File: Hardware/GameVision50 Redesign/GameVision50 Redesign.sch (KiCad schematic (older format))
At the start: 26 parts

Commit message: annotated and assigned footprints
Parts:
- C1, C4: renamed from C?; footprint (none) -> Capacitor_SMD:C_0805_2012Metric
- C10, C2, C3, C7, C8, C9: renamed from C?; footprint (none) -> Capacitor_SMD:C_0402_1005Metric
- C5, C6: renamed from C?; footprint (none) -> Capacitor_SMD:C_0603_1608Metric
- J1, J6: renamed from J?; footprint (none) -> Connector_PinHeader_2.54mm:PinHeader_1x04_P2.54mm_Vertical
- J2: renamed from J?; footprint (none) -> Connector_PinHeader_2.54mm:PinHeader_1x03_P2.54mm_Vertical
- J3: renamed from J?; footprint (none) -> Connector_USB:USB_Mini-B_Lumberg_2486_01_Horizontal
- J4: renamed from J?; footprint (none) -> Connector_PinHeader_2.54mm:PinHeader_1x05_P2.54mm_Vertical
- J5: renamed from J?; footprint (none) -> Connector_JST:JST_XH_B7B-XH-A_1x07_P2.50mm_Vertical
- JP1: renamed from JP?; footprint (none) -> Jumper:SolderJumper-2_P1.3mm_Open_TrianglePad1.0x1.5mm
- R1, R2, R3, R4: renamed from R?; footprint (none) -> Resistor_SMD:R_0402_1005Metric
- R5, R6: renamed from R?; footprint (none) -> Resistor_SMD:R_0603_1608Metric
- Y1: renamed from Y?; footprint (none) -> Crystal:Crystal_SMD_5032-2Pin_5.0x3.2mm
- gave numbers to parts that had none: 2

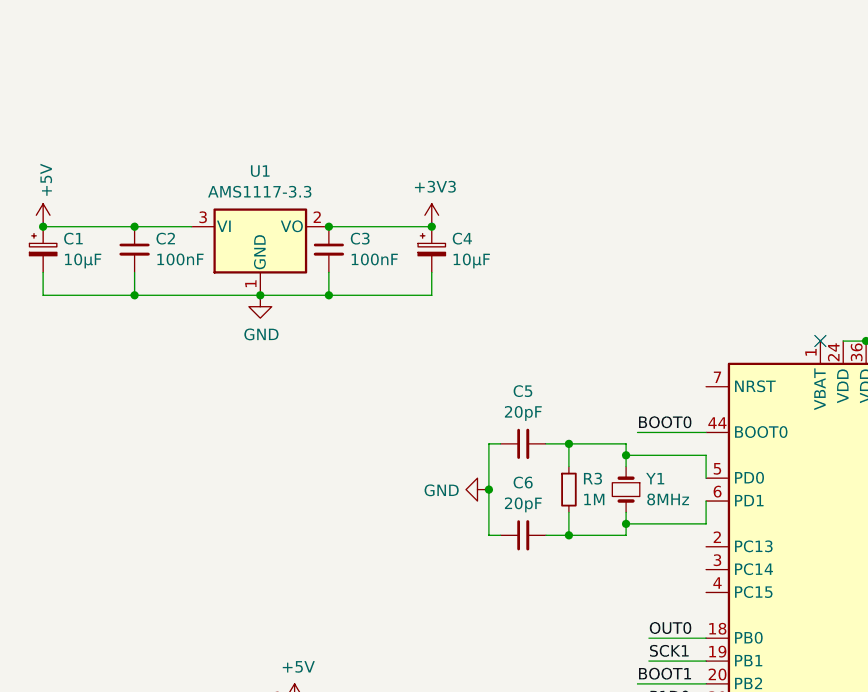
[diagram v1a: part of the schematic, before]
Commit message: added power-on reset IC with pull-up and bypass cap
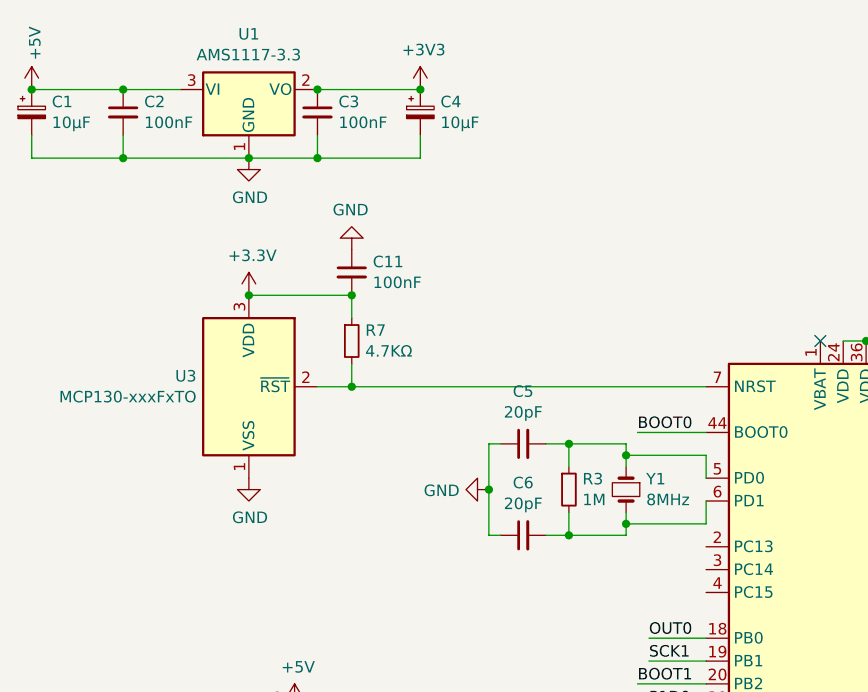
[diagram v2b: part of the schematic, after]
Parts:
- added C11: 100nF, Capacitor_SMD:C_0402_1005Metric, symbol Device:C_Small
- added R7: 4.7KΩ, Resistor_SMD:R_0402_1005Metric, symbol Device:R_Small
- added U3: MCP130-xxxFxTO, Package_TO_SOT_THT:TO-92_Inline, symbol Power_Supervisor:MCP130-xxxFxTO
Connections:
- net +3V3: now also C11.2, R7.1, U3.3 (VDD)
- net GND: now also C11.1, U3.1 (VSS)
- net at U2.7 (NRST): now also R7.2, U3.2 (~RST)
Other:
- moved on the sheet: C1, C2, C3, C4, U1
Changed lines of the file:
@@
 POWER
-$Comp
-L power:+5V #PWR0104
-U 1 1 5EDC21FE
-P 1950 1500
-F 0 "#PWR0104" H 1950 1350 50  0001 C CNN
-F 1 "+5V" V 1965 1628 50  0000 L CNN
-F 2 "" H 1950 1500 50  0001 C CNN
-F 3 "" H 1950 1500 50  0001 C CNN
-	1    1950 1500
-	1    0    0    -1
-$EndComp
-$Comp
-L power:+3V3 #PWR0105
-U 1 1 5EDC2D33
-P 3650 1500
-F 0 "#PWR0105" H 3650 1350 50  0001 C CNN
-F 1 "+3V3" H 3665 1673 50  0000 C CNN
-F 2 "" H 3650 1500 50  0001 C CNN
-F 3 "" H 3650 1500 50  0001 C CNN
-	1    3650 1500
-	1    0    0    -1
-$EndComp
-$Comp
-L Device:CP_Small C1
-U 1 1 5EDC44C0
-P 1950 1600
-F 0 "C1" H 2038 1646 50  0000 L CNN
-F 1 "10μF" H 2038 1555 50  0000 L CNN
-F 2 "Capacitor_SMD:C_0805_2012Metric" H 1950 1600 50  0001 C CNN
-F 3 "~" H 1950 1600 50  0001 C CNN
-F 4 "C15850" H 1950 1600 50  0001 C CNN "LCSC"
-	1    1950 1600
-	1    0    0    -1
-$EndComp
 $Comp
 L Connector_Generic:Conn_01x05 J4
@@
 Text Label 4550 3900 0    50   ~ 0
 RESET
-$Comp
-L Device:C_Small C2
-U 1 1 5EE03D1D
-P 2350 1600
-F 0 "C2" H 2442 1646 50  0000 L CNN
-F 1 "100nF" H 2442 1555 50  0000 L CNN
-F 2 "Capacitor_SMD:C_0402_1005Metric" H 2350 1600 50  0001 C CNN
-F 3 "~" H 2350 1600 50  0001 C CNN
-F 4 "C1525" H 2350 1600 50  0001 C CNN "LCSC"
-	1    2350 1600
-	1    0    0    -1
-$EndComp
-Wire Wire Line
-	3200 1800 3200 1700
-Wire Wire Line
-	3200 1800 3650 1800
-Wire Wire Line
-	3650 1800 3650 1700
-Connection ~ 3200 1800
-Connection ~ 2900 1800
-Wire Wire Line
-	2900 1800 3200 1800
-$Comp
-L power:GND #PWR0114
-U 1 1 5EDC383E
-P 2900 1800
-F 0 "#PWR0114" H 2900 1550 50  0001 C CNN
-F 1 "GND" H 2905 1627 50  0000 C CNN
-F 2 "" H 2900 1800 50  0001 C CNN
-F 3 "" H 2900 1800 50  0001 C CNN
-	1    2900 1800
-	1    0    0    -1
-$EndComp
-$Comp
-L Regulator_Linear:AMS1117-3.3 U1
-U 1 1 5EDBF4D0
-P 2900 1500
-F 0 "U1" H 2900 1742 50  0000 C CNN
-F 1 "AMS1117-3.3" H 2900 1651 50  0000 C CNN
-F 2 "Package_TO_SOT_SMD:SOT-223-3_TabPin2" H 2900 1700 50  0001 C CNN
-F 3 "http://www.advanced-monolithic.com/pdf/ds1117.pdf" H 3000 1250 50  0001 C CNN
-	1    2900 1500
-	1    0    0    -1
-$EndComp
-Wire Wire Line
-	2350 1700 2350 1800
-Wire Wire Line
-	2350 1800 2900 1800
-Wire Wire Line
-	1950 1700 1950 1800
-Wire Wire Line
-	1950 1800 2350 1800
-Connection ~ 2350 1800
-Wire Wire Line
-	1950 1500 2350 1500
-Connection ~ 1950 1500
-Connection ~ 2350 1500
-Wire Wire Line
-	2350 1500 2600 1500
-Wire Wire Line
-	3200 1500 3650 1500
 Text Label 3350 3700 2    50   ~ 0
 POWER
@@
 $EndComp
 $Comp
-L Device:C_Small C3
-U 1 1 5EEB74EE
-P 3200 1600
-F 0 "C3" H 3292 1646 50  0000 L CNN
-F 1 "100nF" H 3292 1555 50  0000 L CNN
-F 2 "Capacitor_SMD:C_0402_1005Metric" H 3200 1600 50  0001 C CNN
-F 3 "~" H 3200 1600 50  0001 C CNN
-F 4 "C1525" H 3200 1600 50  0001 C CNN "LCSC"
-	1    3200 1600
-	1    0    0    -1
-$EndComp
-Connection ~ 3200 1500
-$Comp
 L Device:C_Small C7
 U 1 1 5EEB7BA9
@@
 	0    -1   -1   0
 $EndComp
+Wire Wire Line
+	4550 2400 4850 2400
+$Comp
+L Power_Supervisor:MCP130-xxxFxTO U3
+U 1 1 5EDAF659
+P 2850 2200
+F 0 "U3" H 2621 2246 50  0000 R CNN
+F 1 "MCP130-xxxFxTO" H 2621 2155 50  0000 R CNN
+F 2 "Package_TO_SOT_THT:TO-92_Inline" H 3500 1850 50  0001 C CNN
+F 3 "http://ww1.microchip.com/downloads/en/DeviceDoc/11184d.pdf" H 2850 2200 50  0001 C CNN
+F 4 "C143831" H 2850 2200 50  0001 C CNN "LCSC"
+	1    2850 2200
+	1    0    0    -1
+$EndComp
+$Comp
+L power:GND #PWR02
+U 1 1 5EDB0AB2
+P 2850 2600
+F 0 "#PWR02" H 2850 2350 50  0001 C CNN
+F 1 "GND" H 2855 2427 50  0000 C CNN
+F 2 "" H 2850 2600 50  0001 C CNN
+F 3 "" H 2850 2600 50  0001 C CNN
+	1    2850 2600
+	1    0    0    -1
+$EndComp
+$Comp
+L power:+3.3V #PWR01
+U 1 1 5EDB0F7B
+P 2850 1800
+F 0 "#PWR01" H 2850 1650 50  0001 C CNN
+F 1 "+3.3V" H 2865 1973 50  0000 C CNN
+F 2 "" H 2850 1800 50  0001 C CNN
+F 3 "" H 2850 1800 50  0001 C CNN
+	1    2850 1800
+	1    0    0    -1
+$EndComp
+$Comp
+L Device:R_Small R7
+U 1 1 5EDB3C95
+P 3300 2000
+F 0 "R7" H 3359 2046 50  0000 L CNN
+F 1 "4.7KΩ" H 3359 1955 50  0000 L CNN
+F 2 "Resistor_SMD:R_0402_1005Metric" H 3300 2000 50  0001 C CNN
+F 3 "~" H 3300 2000 50  0001 C CNN
+F 4 "C25900" H 3300 2000 50  0001 C CNN "LCSC"
+	1    3300 2000
+	1    0    0    -1
+$EndComp
+Wire Wire Line
+	2850 1800 3300 1800
+Wire Wire Line
+	3300 1800 3300 1900
+Connection ~ 2850 1800
+Wire Wire Line
+	3150 2200 3300 2200
+Wire Wire Line
+	3300 2200 3300 2100
+Wire Wire Line
+	4850 2200 3300 2200
+Connection ~ 3300 2200
+$Comp
+L power:+5V #PWR0104
+U 1 1 5EDC21FE
+P 1900 900
+F 0 "#PWR0104" H 1900 750 50  0001 C CNN
+F 1 "+5V" V 1915 1028 50  0000 L CNN
+F 2 "" H 1900 900 50  0001 C CNN
+F 3 "" H 1900 900 50  0001 C CNN
+	1    1900 900
+	1    0    0    -1
+$EndComp
+$Comp
+L power:+3V3 #PWR0105
+U 1 1 5EDC2D33
+P 3600 900
+F 0 "#PWR0105" H 3600 750 50  0001 C CNN
+F 1 "+3V3" H 3615 1073 50  0000 C CNN
+F 2 "" H 3600 900 50  0001 C CNN
+F 3 "" H 3600 900 50  0001 C CNN
+	1    3600 900
+	1    0    0    -1
+$EndComp
+$Comp
+L Device:CP_Small C1
+U 1 1 5EDC44C0
+P 1900 1000
+F 0 "C1" H 1988 1046 50  0000 L CNN
+F 1 "10μF" H 1988 955 50  0000 L CNN
+F 2 "Capacitor_SMD:C_0805_2012Metric" H 1900 1000 50  0001 C CNN
+F 3 "~" H 1900 1000 50  0001 C CNN
+F 4 "C15850" H 1900 1000 50  0001 C CNN "LCSC"
+	1    1900 1000
+	1    0    0    -1
+$EndComp
+$Comp
+L Device:C_Small C2
+U 1 1 5EE03D1D
+P 2300 1000
+F 0 "C2" H 2392 1046 50  0000 L CNN
+F 1 "100nF" H 2392 955 50  0000 L CNN
+F 2 "Capacitor_SMD:C_0402_1005Metric" H 2300 1000 50  0001 C CNN
+F 3 "~" H 2300 1000 50  0001 C CNN
+F 4 "C1525" H 2300 1000 50  0001 C CNN "LCSC"
+	1    2300 1000
+	1    0    0    -1
+$EndComp
+Wire Wire Line
+	3150 1200 3150 1100
+Wire Wire Line
+	3150 1200 3600 1200
+Wire Wire Line
+	3600 1200 3600 1100
+Connection ~ 3150 1200
+Connection ~ 2850 1200
+Wire Wire Line
+	2850 1200 3150 1200
+$Comp
+L power:GND #PWR0114
+U 1 1 5EDC383E
+P 2850 1200
+F 0 "#PWR0114" H 2850 950 50  0001 C CNN
+F 1 "GND" H 2855 1027 50  0000 C CNN
+F 2 "" H 2850 1200 50  0001 C CNN
+F 3 "" H 2850 1200 50  0001 C CNN
+	1    2850 1200
+	1    0    0    -1
+$EndComp
+$Comp
+L Regulator_Linear:AMS1117-3.3 U1
+U 1 1 5EDBF4D0
+P 2850 900
+F 0 "U1" H 2850 1142 50  0000 C CNN
+F 1 "AMS1117-3.3" H 2850 1051 50  0000 C CNN
+F 2 "Package_TO_SOT_SMD:SOT-223-3_TabPin2" H 2850 1100 50  0001 C CNN
+F 3 "http://www.advanced-monolithic.com/pdf/ds1117.pdf" H 2950 650 50  0001 C CNN
+	1    2850 900
+	1    0    0    -1
+$EndComp
+Wire Wire Line
+	2300 1100 2300 1200
+Wire Wire Line
+	2300 1200 2850 1200
+Wire Wire Line
+	1900 1100 1900 1200
+Wire Wire Line
+	1900 1200 2300 1200
+Connection ~ 2300 1200
+Wire Wire Line
+	1900 900  2300 900
+Connection ~ 1900 900
+Connection ~ 2300 900
+Wire Wire Line
+	2300 900  2550 900
+Wire Wire Line
+	3150 900  3600 900
+$Comp
+L Device:C_Small C3
+U 1 1 5EEB74EE
+P 3150 1000
+F 0 "C3" H 3242 1046 50  0000 L CNN
+F 1 "100nF" H 3242 955 50  0000 L CNN
+F 2 "Capacitor_SMD:C_0402_1005Metric" H 3150 1000 50  0001 C CNN
+F 3 "~" H 3150 1000 50  0001 C CNN
+F 4 "C1525" H 3150 1000 50  0001 C CNN "LCSC"
+	1    3150 1000
+	1    0    0    -1
+$EndComp
+Connection ~ 3150 900
 $Comp
 L Device:CP_Small C4
 U 1 1 5EEC946A
-P 3650 1600
-F 0 "C4" H 3738 1646 50  0000 L CNN
-F 1 "10μF" H 3738 1555 50  0000 L CNN
-F 2 "Capacitor_SMD:C_0805_2012Metric" H 3650 1600 50  0001 C CNN
-F 3 "~" H 3650 1600 50  0001 C CNN
-F 4 "C15850" H 3650 1600 50  0001 C CNN "LCSC"
-	1    3650 1600
-	1    0    0    -1
-$EndComp
-Connection ~ 3650 1500
-Wire Wire Line
-	4550 2400 4850 2400
+P 3600 1000
+F 0 "C4" H 3688 1046 50  0000 L CNN
+F 1 "10μF" H 3688 955 50  0000 L CNN
+F 2 "Capacitor_SMD:C_0805_2012Metric" H 3600 1000 50  0001 C CNN
+F 3 "~" H 3600 1000 50  0001 C CNN
+F 4 "C15850" H 3600 1000 50  0001 C CNN "LCSC"
+	1    3600 1000
+	1    0    0    -1
+$EndComp
+Connection ~ 3600 900
+$Comp
+L power:GND #PWR03
+U 1 1 5EDE0288
+P 3300 1600
+F 0 "#PWR03" H 3300 1350 50  0001 C CNN
+F 1 "GND" H 3305 1427 50  0000 C CNN
+F 2 "" H 3300 1600 50  0001 C CNN
+F 3 "" H 3300 1600 50  0001 C CNN
+	1    3300 1600
+	-1   0    0    1
+$EndComp
+$Comp
+L Device:C_Small C11
+U 1 1 5EDE028F
+P 3300 1700
+F 0 "C11" H 3392 1746 50  0000 L CNN
+F 1 "100nF" H 3392 1655 50  0000 L CNN
+F 2 "Capacitor_SMD:C_0402_1005Metric" H 3300 1700 50  0001 C CNN
+F 3 "~" H 3300 1700 50  0001 C CNN
+F 4 "C1525" H 3300 1700 50  0001 C CNN "LCSC"
+	1    3300 1700
+	1    0    0    -1
+$EndComp
+Connection ~ 3300 1800
 $EndSCHEMATC
